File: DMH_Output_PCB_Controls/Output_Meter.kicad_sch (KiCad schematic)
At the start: 63 parts, among them Q1 BC558, Q2 BC558, U1 TL072, U2 LM339, U3 LM339, U4 LM339, U5 LM339, U6 LM339

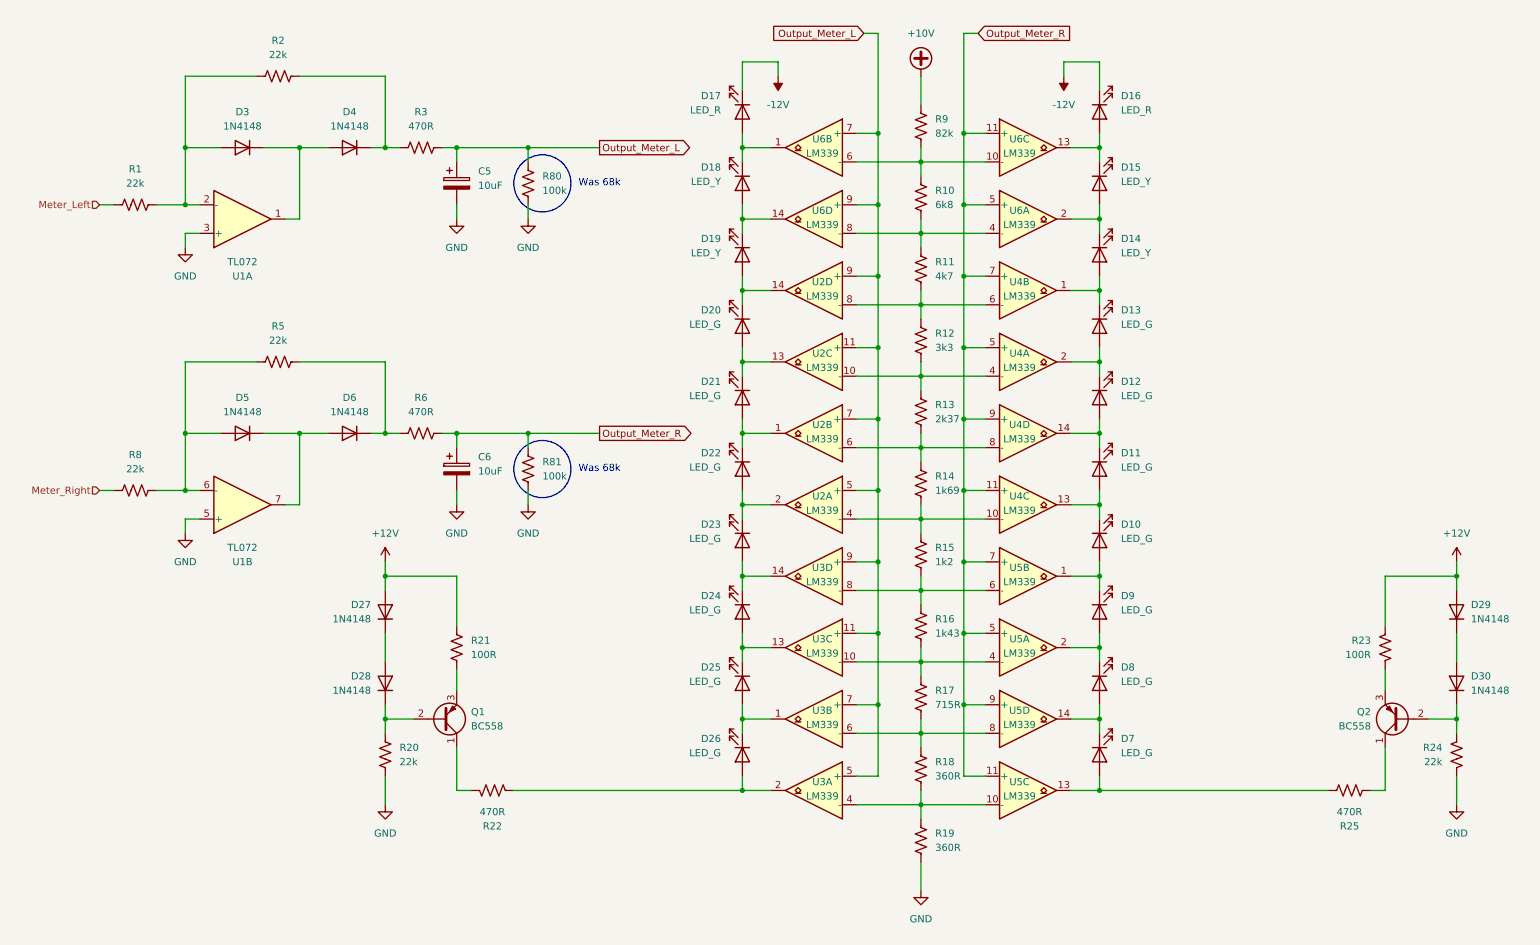
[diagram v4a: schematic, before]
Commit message: Clarifying inter PCB connectors in progress
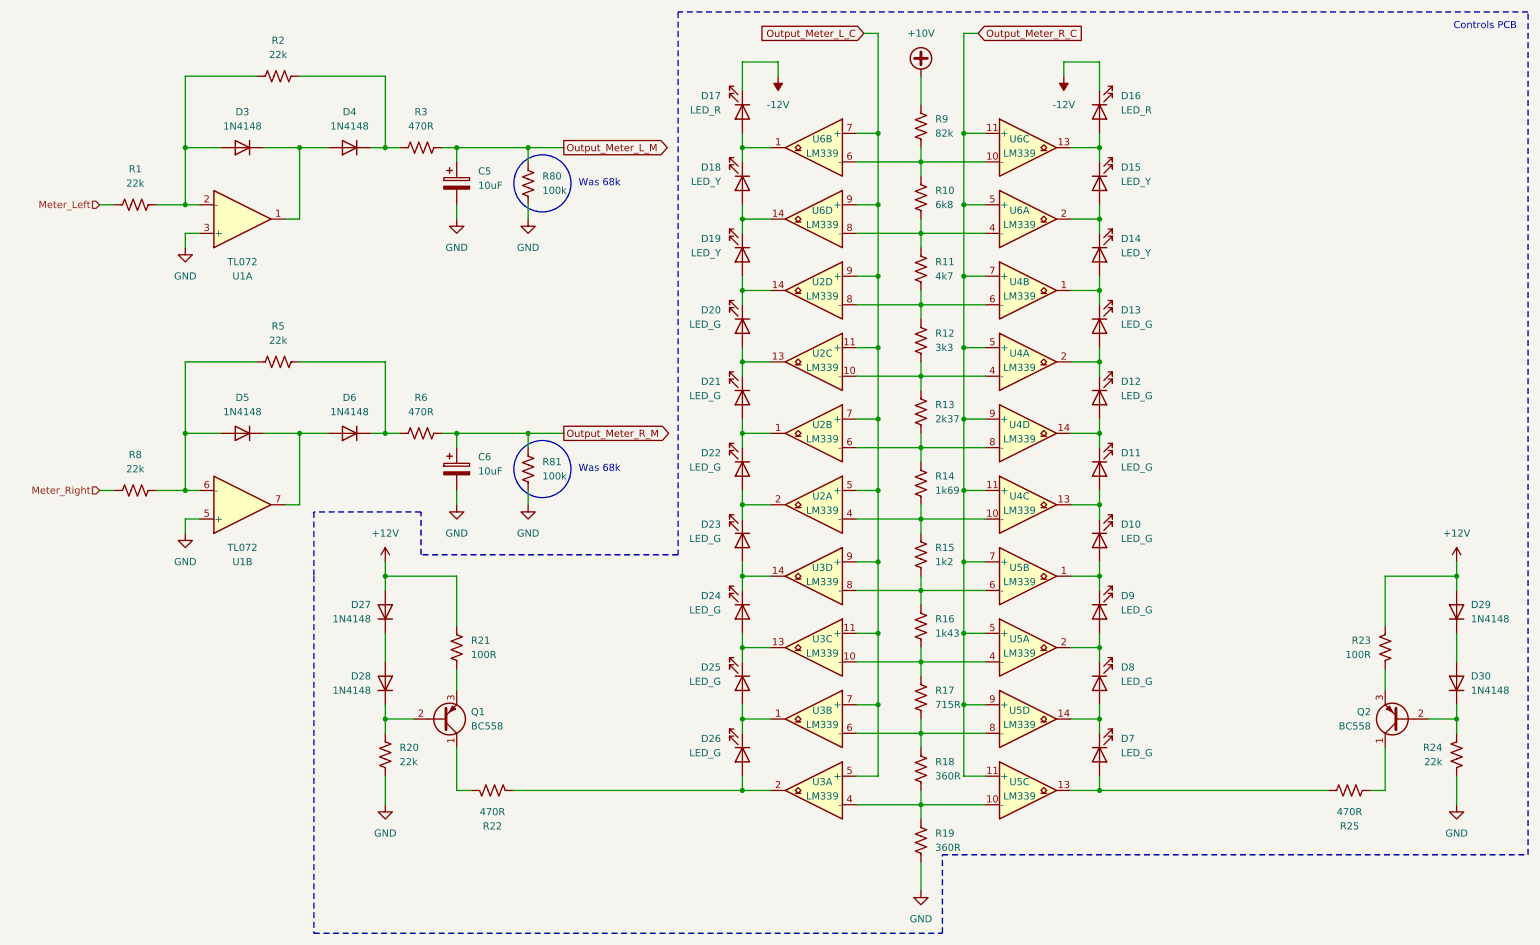
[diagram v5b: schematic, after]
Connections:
- net Output_Meter_L renamed Output_Meter_L_C
- net Output_Meter_L_C: no longer C5.1, R3.2, R80.2
- net Output_Meter_R renamed Output_Meter_R_C
- net Output_Meter_R_C: no longer C6.1, R6.2, R81.2
- new net Output_Meter_L_M: C5.1, R3.2, R80.2
- new net Output_Meter_R_M: C6.1, R6.2, R81.2
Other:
- note added: "Controls PCB"
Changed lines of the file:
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@@
+		)
+	)
+	(text "Controls PCB"
+		(exclude_from_sim no)
+		(at 271.78 16.51 0)
+		(effects
+			(font
+				(size 1.27 1.27)
+			)
 		)
 	)
@@
 		)
 	)
+	(polyline
+		(pts
+			(xy 175.26 177.8) (xy 175.26 163.83)
+		)
+		(stroke
+			(width 0.25)
+			(type dash)
+		)
+	)
 	(wire
 		(pts
@@
 		)
 	)
+	(polyline
+		(pts
+			(xy 128.27 110.49) (xy 82.55 110.49)
+		)
+		(stroke
+			(width 0.25)
+			(type dash)
+		)
+	)
 	(wire
 		(pts
@@
 	(wire
 		(pts
-			(xy 101.6 38.1) (xy 114.3 38.1)
-		)
-		(stroke
-			(width 0)
-			(type default)
+			(xy 101.6 38.1) (xy 107.95 38.1)
+		)
+		(stroke
+			(width 0)
+			(type default)
+		)
+	)
+	(polyline
+		(pts
+			(xy 82.55 110.49) (xy 82.55 102.87)
+		)
+		(stroke
+			(width 0.25)
+			(type dash)
+		)
+	)
+	(polyline
+		(pts
+			(xy 63.5 114.3) (xy 63.5 177.8)
+		)
+		(stroke
+			(width 0.25)
+			(type dash)
 		)
 	)
@@
 		)
 	)
+	(polyline
+		(pts
+			(xy 63.5 102.87) (xy 63.5 114.3)
+		)
+		(stroke
+			(width 0.25)
+			(type dash)
+		)
+	)
 	(wire
 		(pts
@@
 	(wire
 		(pts
-			(xy 101.6 88.9) (xy 114.3 88.9)
+			(xy 101.6 88.9) (xy 107.95 88.9)
 		)
 		(stroke
@@
 		)
 	)
+	(polyline
+		(pts
+			(xy 279.4 163.83) (xy 279.4 13.97)
+		)
+		(stroke
+			(width 0.25)
+			(type dash)
+		)
+	)
 	(wire
 		(pts
@@
 		)
 	)
+	(polyline
+		(pts
+			(xy 175.26 163.83) (xy 279.4 163.83)
+		)
+		(stroke
+			(width 0.25)
+			(type dash)
+		)
+	)
 	(wire
 		(pts
@@
 		)
 	)
+	(polyline
+		(pts
+			(xy 128.27 13.97) (xy 128.27 110.49)
+		)
+		(stroke
+			(width 0.25)
+			(type dash)
+		)
+	)
 	(wire
 		(pts
@@
 		)
 	)
+	(polyline
+		(pts
+			(xy 82.55 102.87) (xy 63.5 102.87)
+		)
+		(stroke
+			(width 0.25)
+			(type dash)
+		)
+	)
 	(wire
 		(pts
@@
 		)
 	)
+	(polyline
+		(pts
+			(xy 279.4 13.97) (xy 128.27 13.97)
+		)
+		(stroke
+			(width 0.25)
+			(type dash)
+		)
+	)
 	(wire
 		(pts
@@
 		)
 	)
+	(polyline
+		(pts
+			(xy 63.5 177.8) (xy 175.26 177.8)
+		)
+		(stroke
+			(width 0.25)
+			(type dash)
+		)
+	)
 	(wire
 		(pts
@@
 		)
 	)
-	(global_label "Output_Meter_L"
+	(global_label "Output_Meter_L_M"
 		(shape output)
-		(at 114.3 38.1 0)
+		(at 107.95 38.1 0)
 		(fields_autoplaced yes)
 		(effects
@@
 		)
 		(property "Intersheetrefs" "${INTERSHEET_REFS}"
-			(at 131.6179 38.1 0)
+			(at 127.6869 38.1 0)
 			(effects
 				(font
@@
 		)
 	)
-	(global_label "Output_Meter_L"
+	(global_label "Output_Meter_L_C"
 		(shape input)
 		(at 161.29 17.78 180)
@@
 		)
 		(property "Intersheetrefs" "${INTERSHEET_REFS}"
-			(at 143.9721 17.78 0)
+			(at 141.7345 17.78 0)
 			(effects
 				(font
@@
 		)
 	)
-	(global_label "Output_Meter_R"
+	(global_label "Output_Meter_R_M"
 		(shape output)
-		(at 114.3 88.9 0)
+		(at 107.95 88.9 0)
 		(fields_autoplaced yes)
 		(effects
@@
 		)
 		(property "Intersheetrefs" "${INTERSHEET_REFS}"
-			(at 131.8598 88.9 0)
+			(at 127.9288 88.9 0)
 			(effects
 				(font
@@
 		)
 	)
-	(global_label "Output_Meter_R"
+	(global_label "Output_Meter_R_C"
 		(shape input)
 		(at 181.61 17.78 0)
@@
 		)
 		(property "Intersheetrefs" "${INTERSHEET_REFS}"
-			(at 199.1698 17.78 0)
+			(at 201.4074 17.78 0)
 			(effects
 				(font

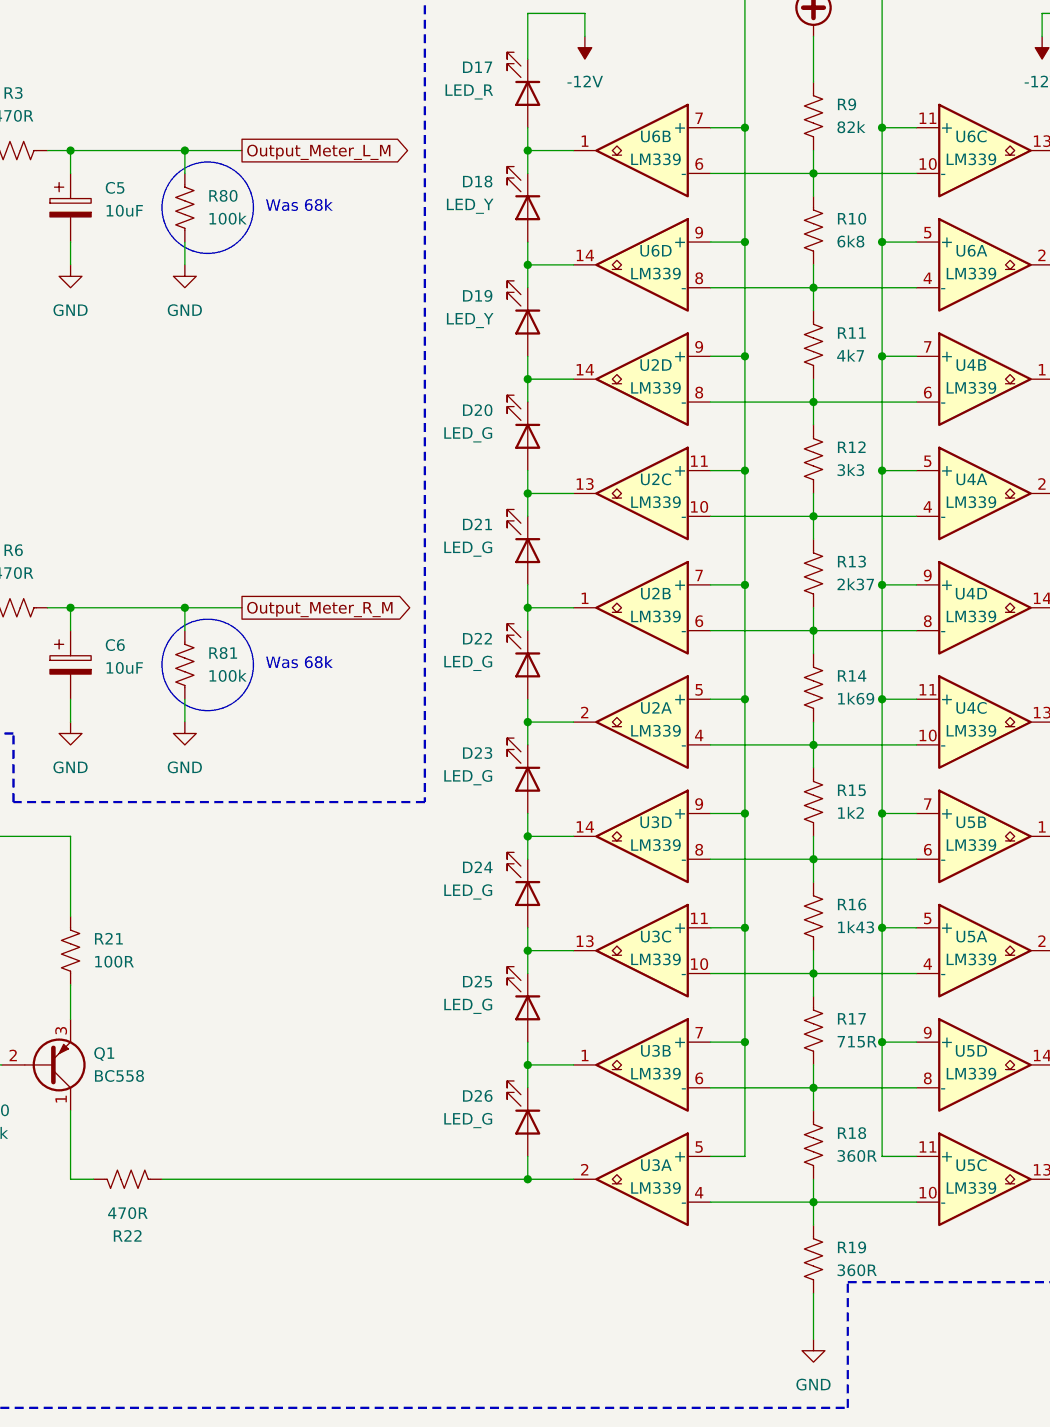
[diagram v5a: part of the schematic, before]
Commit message: Adjustments during prototyping
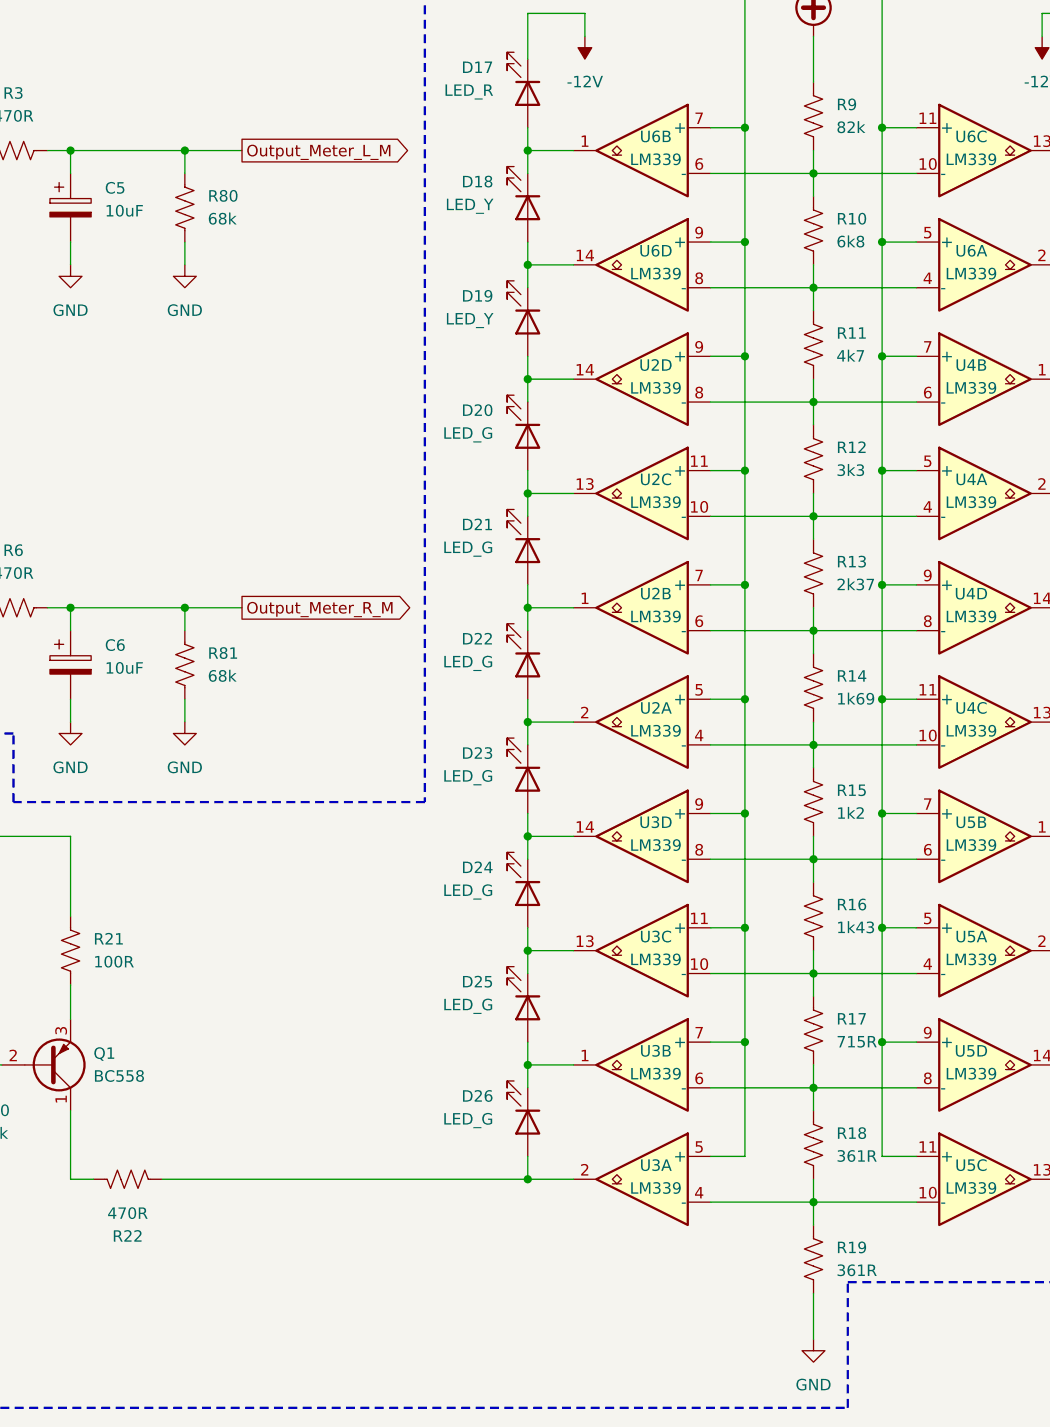
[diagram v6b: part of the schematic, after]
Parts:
- R18, R19: value 360R -> 361R
- R80, R81: value 100k -> 68k
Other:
- note removed: "Was 68k"
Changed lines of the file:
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@@
 		(comment 1 "PCB for 5 cm Kosmo format synthesizer module")
 	)
-	(circle
-		(center 104.14 95.25)
-		(radius 5.08)
-		(stroke
-			(width 0)
-			(type default)
-		)
-		(fill
-			(type none)
-		)
-	)
-	(circle
-		(center 104.14 44.45)
-		(radius 5.08)
-		(stroke
-			(width 0)
-			(type default)
-		)
-		(fill
-			(type none)
-		)
-	)
-	(text "Was 68k"
-		(exclude_from_sim no)
-		(at 114.3 44.45 0)
-		(effects
-			(font
-				(size 1.27 1.27)
-			)
-		)
-	)
 	(text "Controls PCB"
 		(exclude_from_sim no)
@@
 		)
 	)
-	(text "Was 68k"
-		(exclude_from_sim no)
-		(at 114.3 95.25 0)
-		(effects
-			(font
-				(size 1.27 1.27)
-			)
-		)
-	)
 	(junction
 		(at 139.7 139.7)
@@
 			)
 		)
-		(property "Value" "100k"
+		(property "Value" "68k"
 			(at 104.14 45.7199 0)
 			(effects
@@
 			)
 		)
-		(property "Value" "360R"
+		(property "Value" "361R"
 			(at 173.99 149.8599 0)
 			(effects
@@
 			)
 		)
-		(property "Value" "100k"
+		(property "Value" "68k"
 			(at 104.14 96.5199 0)
 			(effects
@@
 			)
 		)
-		(property "Value" "360R"
+		(property "Value" "361R"
 			(at 173.99 162.5599 0)
 			(effects

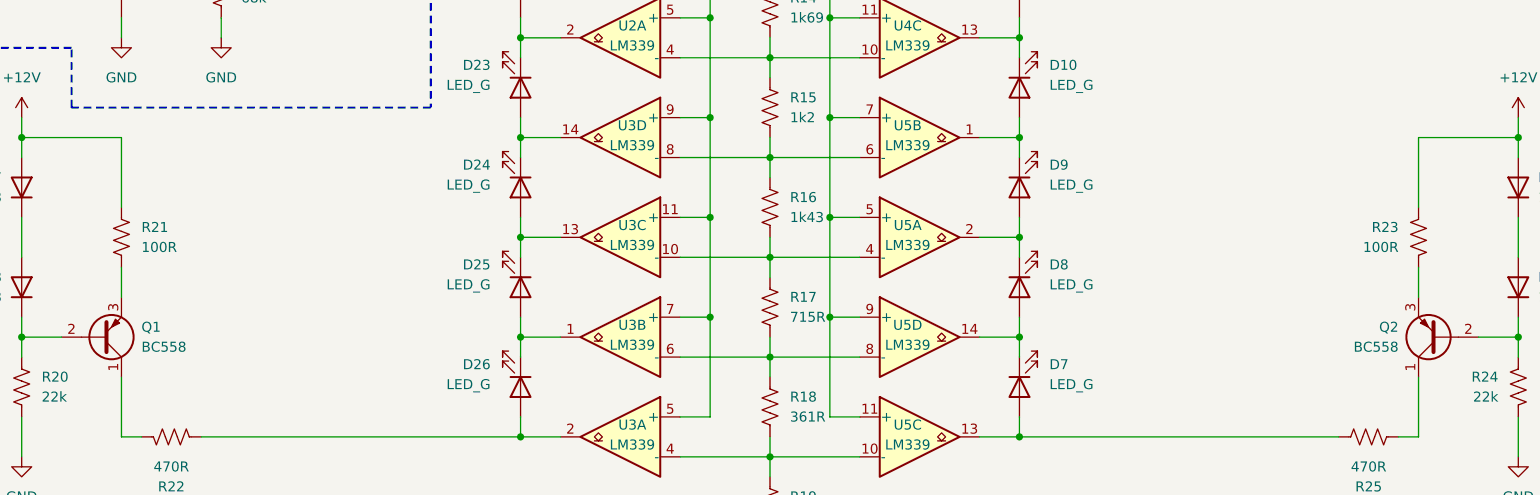
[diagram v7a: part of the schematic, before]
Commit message: Replaced jack symbols with 5pin ones
Also updated Meter LED current source resistor to 75R
Also increased LED guiding PCB mounting holes to M2.5
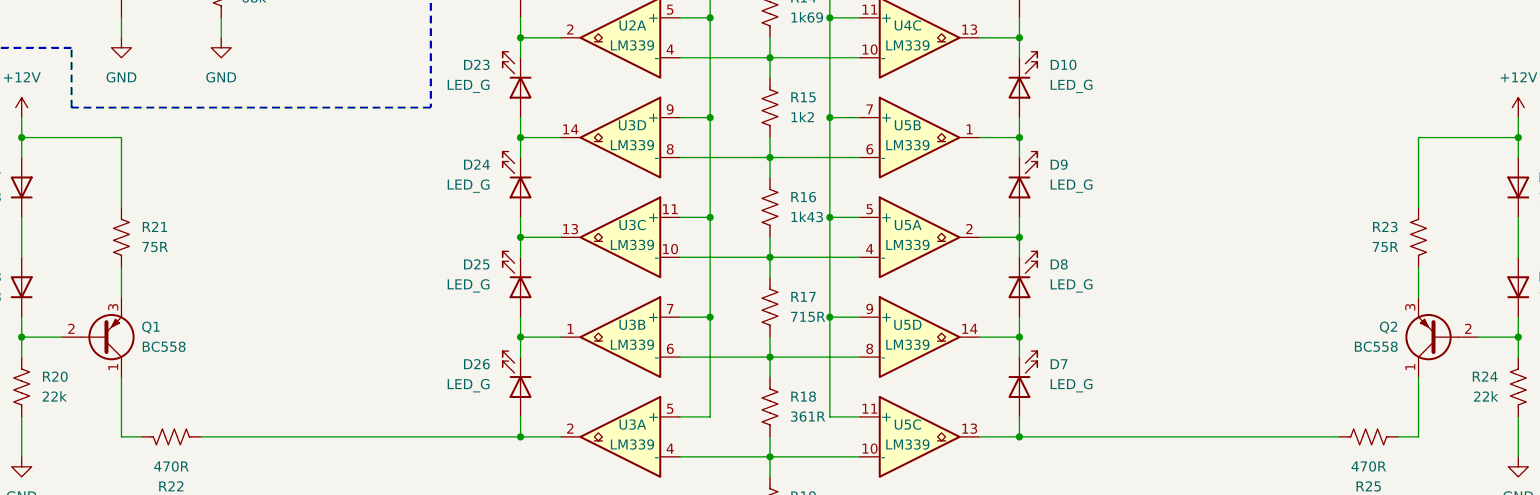
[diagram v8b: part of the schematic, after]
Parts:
- R21, R23: value 100R -> 75R
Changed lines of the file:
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@@
 			)
 		)
-		(property "Value" "100R"
+		(property "Value" "75R"
 			(at 251.46 128.2699 0)
 			(show_name no)
@@
 			)
 		)
-		(property "Value" "100R"
+		(property "Value" "75R"
 			(at 91.44 128.2699 0)
 			(show_name no)
